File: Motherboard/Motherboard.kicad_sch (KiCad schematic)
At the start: 52 parts, among them J1 Conn_01x01, J10 ATX-24, J11 USB_B, J12 Bus_ISA_8bit, J13 65SIB_Connector, J2 Conn_01x01, J3 Conn_01x01, J4 Conn_01x01, J9 Bus_ISA_8bit, SW1 SW_Push, SW2 SW_SPST, U1 SC28L91, U10 XCR3064XL-VQ100, U12 LM7905_TO220, U13 MCP2200-I-SO, U14 74HCT163, U15 74HCT137, U2 AS6C1608, U3 WD65C22, U4 SST39SF040, U5 SST39SF040, U6 WD65C816S, U7 DS1813, U8 74HCT245, U9 74HCT573, X1 ACO-3.6864MHz, X2 ACO-24MHz, X3 ACO-14.31818MHz

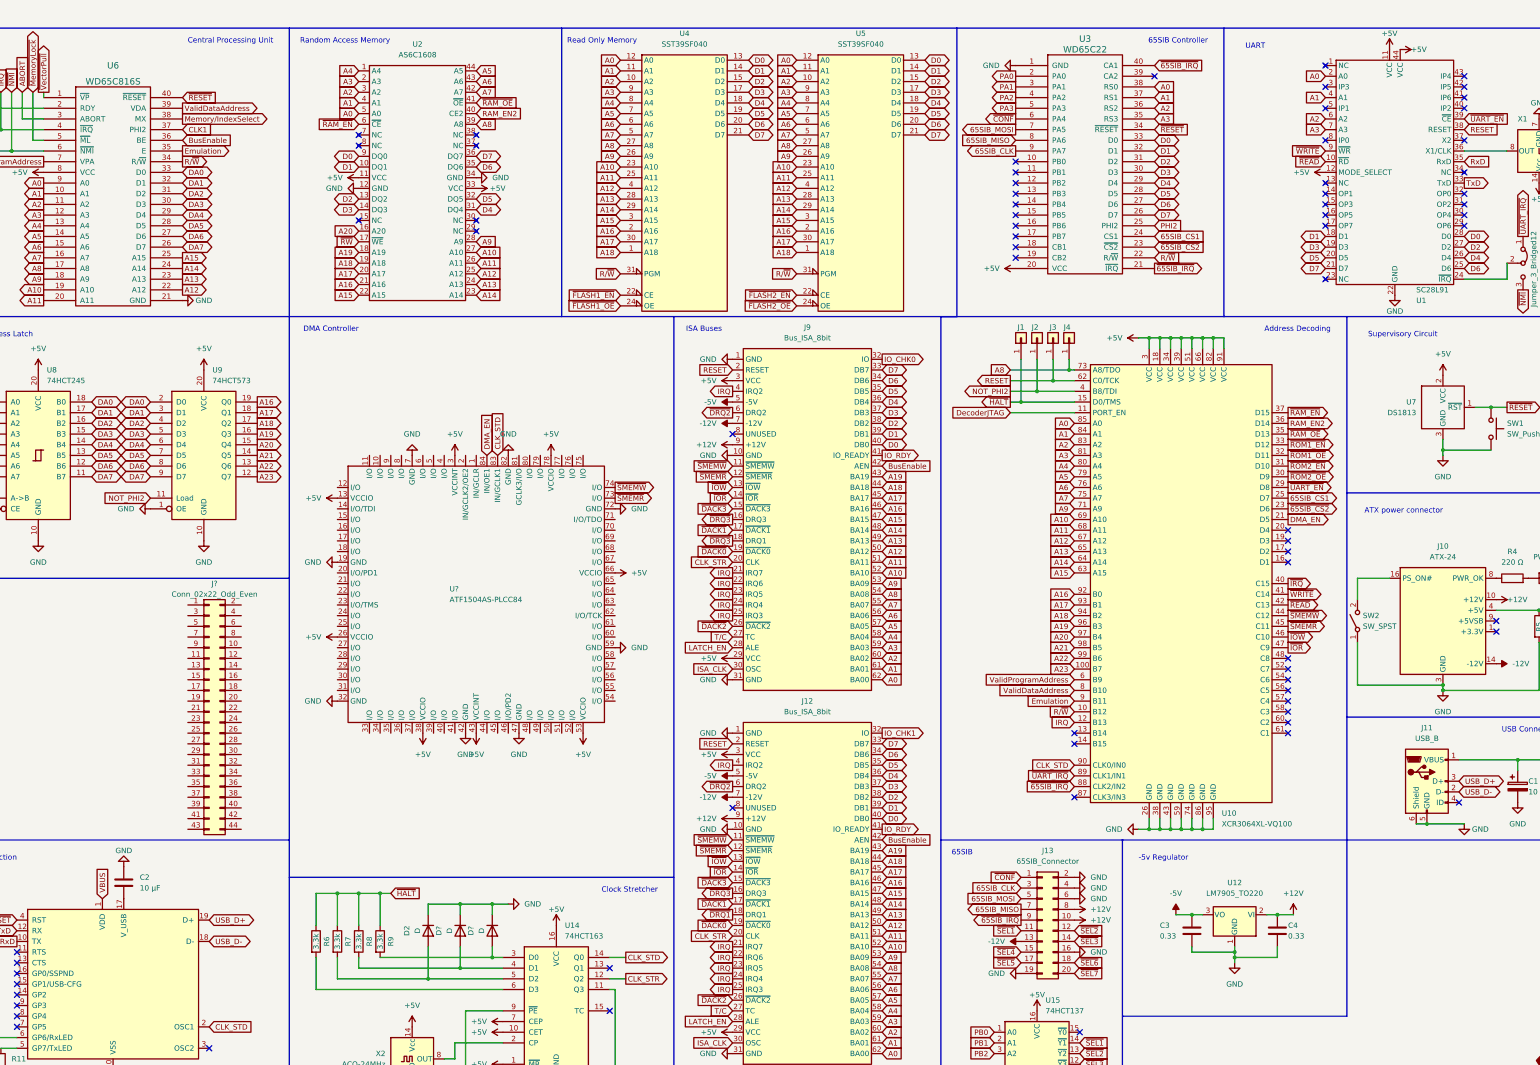
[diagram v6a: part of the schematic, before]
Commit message: Update Motherboard.kicad_sch
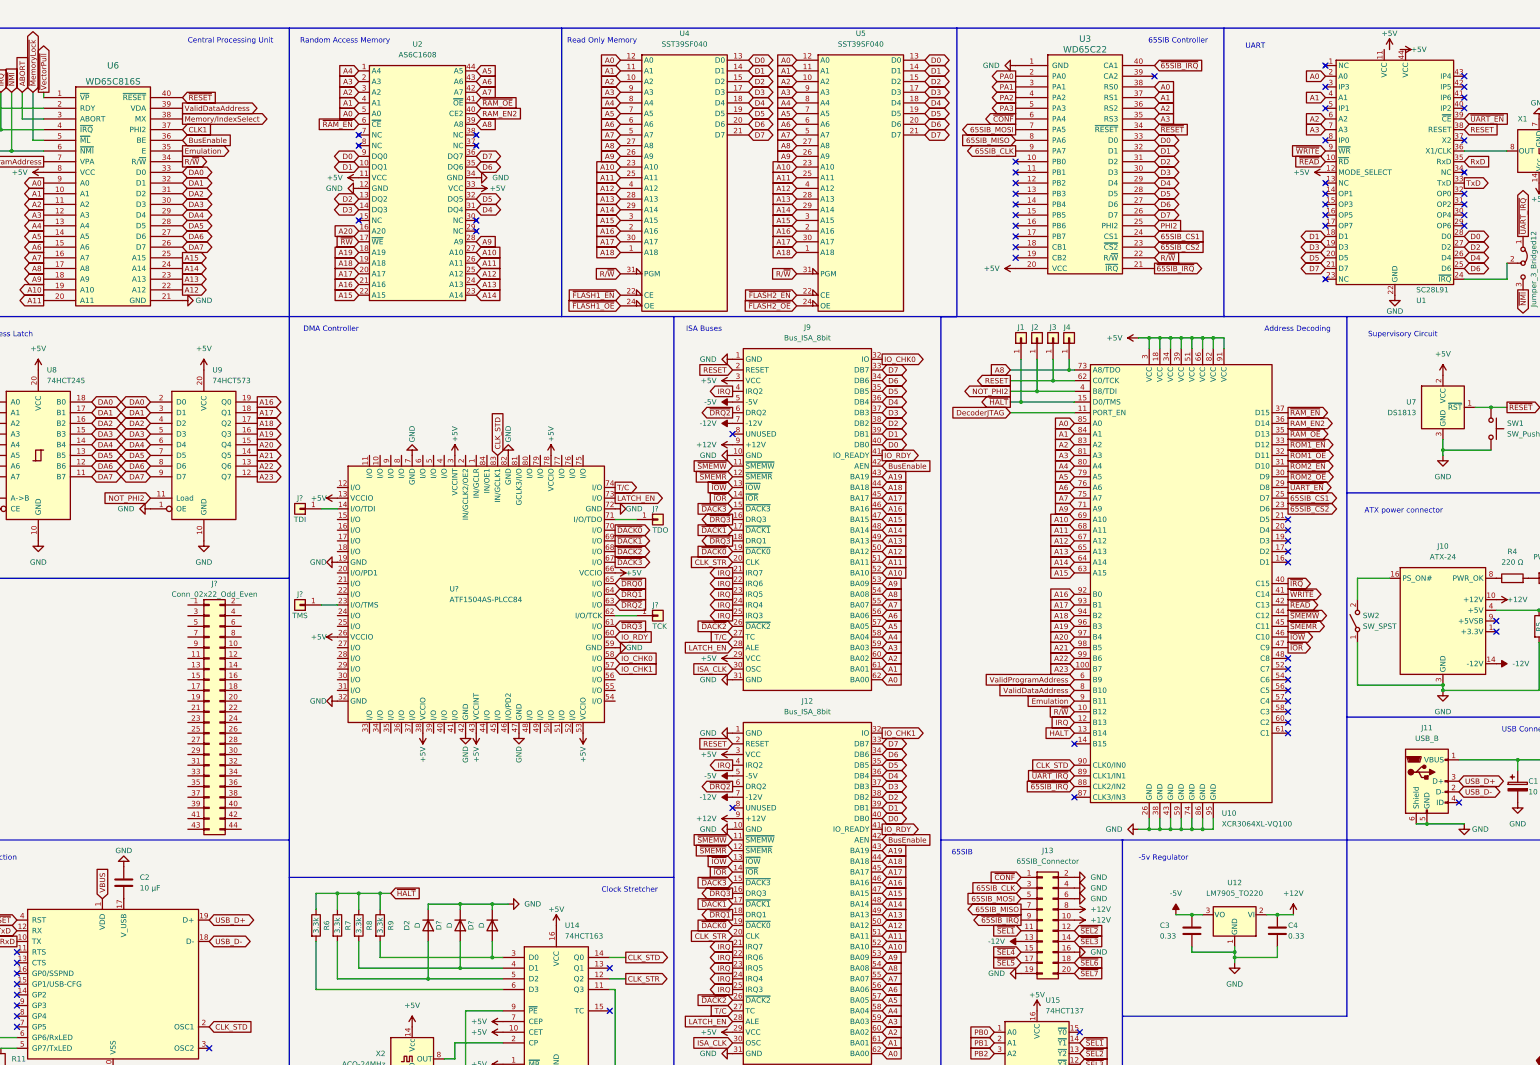
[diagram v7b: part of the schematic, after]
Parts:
- added J?: TDO, symbol Connector_Generic:Conn_01x01
- added J?: TMS, symbol Connector_Generic:Conn_01x01
- added J?: TCK, symbol Connector_Generic:Conn_01x01
- added J?: TDI, symbol Connector_Generic:Conn_01x01
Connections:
- net +5V: no longer U1.11 (VCC), U1.44 (VCC)
- net IO_CHK0: now also U?.58 (I/O)
- net IO_CHK1: now also U?.57 (I/O)
- net IO_RDY: now also U?.60 (I/O)
- net LATCH_EN: now also U?.73 (I/O)
- net T/C: now also U?.74 (I/O)
- net ~{DACK0}: now also U?.70 (I/O)
- net ~{DACK1}: now also U?.69 (I/O)
- net ~{DACK2}: now also U?.68 (I/O)
- net ~{DACK3}: now also U?.67 (I/O)
- net ~{DRQ1}: now also U?.64 (I/O)
- net ~{DRQ2}: now also U?.63 (I/O)
- net ~{DRQ3}: now also U?.61 (I/O)
- net ~{SMEMR}: no longer U?.73 (I/O)
- net ~{SMEMW}: no longer U?.74 (I/O)
- net at U?.14 (I/O/TDI): now also J?.1 (Pin_1)
- net at U?.23 (I/O/TMS): now also J?.1 (Pin_1)
- net at U?.62 (I/O/TCK): now also J?.1 (Pin_1)
- net ~{DRQ0}: now reaches U?.65 (I/O)
- net at U?.71 (I/O/TDO): now also J?.1 (Pin_1)
- net HALT: now reaches U10.13 (B14)
- net DMA_EN: no longer names the net of U?.84 (IN/OE1)
- net DMA_EN: no longer U10.21 (D5)
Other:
- moved on the sheet: D2, D?, R6, R7, R8, R9

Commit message: Update Motherboard.kicad_sch
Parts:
- removed J1, J2, J3, J4: Conn_01x01, Connector_Pin:Pin_D1.0mm_L10.0mm, symbol Connector_Generic:Conn_01x01
- removed J?: TDO, symbol Connector_Generic:Conn_01x01
- removed J?: TMS, symbol Connector_Generic:Conn_01x01
- removed J?: TCK, symbol Connector_Generic:Conn_01x01
- removed J?: TDI, symbol Connector_Generic:Conn_01x01
- removed U10: XCR3064XL-VQ100, Package_QFP:LQFP-100_14x14mm_P0.5mm, symbol CPLD_Xilinx:XCR3064XL-VQ100
- added J?: ATF15XX_JTAG_ISP, symbol Interfaces:ATF15XX_JTAG_ISP
- J1: renamed from J?; value Conn_02x22_Odd_Even -> 40-pin IDE Connector; footprint (none) -> Connector_PinHeader_2.54mm:PinHeader_2x20_P2.54mm_Vertical; symbol Connector_Generic:Conn_02x22_Odd_Even -> Connector_Generic:Conn_02x20_Odd_Even
- J3: renamed from J9; footprint (none) -> Connector_PinSocket_1.00mm:PinSocket_2x31_P1.00mm_Vertical_SMD
- J9: renamed from J12; footprint (none) -> Connector_PinSocket_1.00mm:PinSocket_2x31_P1.00mm_Vertical_SMD
- gave numbers to parts that had none: 3
- renumbered D3 to D5, D4 to D6, J13 to J10, J10 to J7, J11 to J8, U12 to U11, U13 to U12, U14 to U13, U15 to U14
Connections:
- net ~{FLASH1_OE} is gone; now on net ~{READ}: U4.24 (OE)
- net ~{FLASH2_OE} is gone; now on net ~{READ}: U5.24 (OE)
- net ~{RAM_OE} is gone; now on net ~{READ}: U2.41 (~{OE})
- net ~{RW} is gone; now on net ~{WRITE}: U2.17 (~{WE})
- net +5V: now also J?.4 (VCC)
- net 65SIB_CS1: now also U10.6 (I/O)
- net A0: now also U10.12 (I/O)
- net A1: now also U10.15 (I/O)
- net A10: now also U10.27 (I/O)
- net A11: now also U10.28 (I/O)
- net A12: now also U10.29 (I/O)
- net A13: now also U10.30 (I/O)
- net A14: now also U10.31 (I/O)
- net A15: now also U10.33 (I/O)
- net A16: now also U10.34 (I/O)
- net A17: now also U10.35 (I/O)
- net A18: now also U10.36 (I/O)
- net A19: now also U10.37 (I/O)
- net A2: now also U10.16 (I/O)
- net A20: now also U10.39 (I/O)
- net A21: now also U10.40 (I/O)
- net A22: now also U10.41 (I/O)
- net A23: now also U10.44 (I/O)
- net A3: now also U10.17 (I/O)
- net A4: now also U10.18 (I/O)
- net A5: now also U10.20 (I/O/PD1)
- net A6: now also U10.21 (I/O)
- net A7: now also U10.22 (I/O)
- net A8: now also U10.24 (I/O)
- net A9: now also U10.25 (I/O)
- net Emulation: now also U10.48 (I/O)
- net GND: now also J?.10 (GND), J?.2 (GND)
- net HALT: now also U10.81 (GCLK3/I/O)
- net IO_CHK0: now also U10.1 (IN/GCLR); no longer U10.58 (I/O)
- net IO_CHK1: now also U10.84 (IN/OE1); no longer U10.57 (I/O)
- net IRQ: now also U10.54 (I/O)
- net NOT_PHI2: now also U10.49 (I/O)
- net RAM_EN2: now also U10.10 (I/O)
- net RESET: now also U10.50 (I/O)
- net R/~{W}: now also U10.2 (IN/GCLK2/OE2); no longer U4.31 (PGM), U5.31 (PGM)
- net ValidDataAddress: now also U10.46 (I/O/PD2)
- net ValidProgramAddress: now also U10.45 (I/O)
- net ~{65SIB_CS2}: now also U10.5 (I/O)
- net ~{65SIB_IRQ}: now also U10.56 (I/O)
- net ~{FLASH1_EN}: now also U10.58 (I/O)
- net ~{FLASH2_EN}: now also U10.57 (I/O)
- net ~{HALT}: now also U10.4 (I/O)
- net ~{IOR}: now also U10.51 (I/O)
- net ~{IOW}: now also U10.52 (I/O)
- net ~{IRQ}: now also U10.75 (I/O)
- net ~{RAM_EN}: now also U10.11 (I/O)
- net ~{READ}: now also U10.76 (I/O)
- net ~{RESET}: now also U10.9 (I/O)
- net ~{SMEMR}: now also U10.79 (I/O)
- net ~{SMEMW}: now also U10.80 (I/O)
- net ~{UART_EN}: now also U10.8 (I/O)
- net ~{UART_IRQ}: now also U10.55 (I/O)
- net ~{WRITE}: now also U10.77 (I/O), U4.31 (PGM), U5.31 (PGM)
- net TDI: now reaches U10.14 (I/O/TDI)
- net TDI: now also J?.9 (TDI)
- net TMS: now reaches U10.23 (I/O/TMS)
- net TMS: now also J?.5 (TMS)
- net TCK: now reaches U10.62 (I/O/TCK)
- net TCK: now also J?.1 (TCK)
- net TDO: now reaches U10.71 (I/O/TDO)
- net TDO: now also J?.3 (TDO)
- no-connect marks 70 -> 58
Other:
- note added: "Address Decoder and DMA Controller"
- note added: "IDE Controller"
- note removed: "Address Decoding"
- note removed: "DMA Controller"
- moved on the sheet: U10
